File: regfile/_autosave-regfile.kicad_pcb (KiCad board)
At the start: 2 copper layers, 105.5 x 100 mm, 17 parts, among them J1 Conn_01x39_Pin, U1 74LS170, U1 74LS670, U11 74LS670, U12 74LS670, U13 74LS670, U14 74LS670, U18 74LS170, U2 74LS170, U2 74LS670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

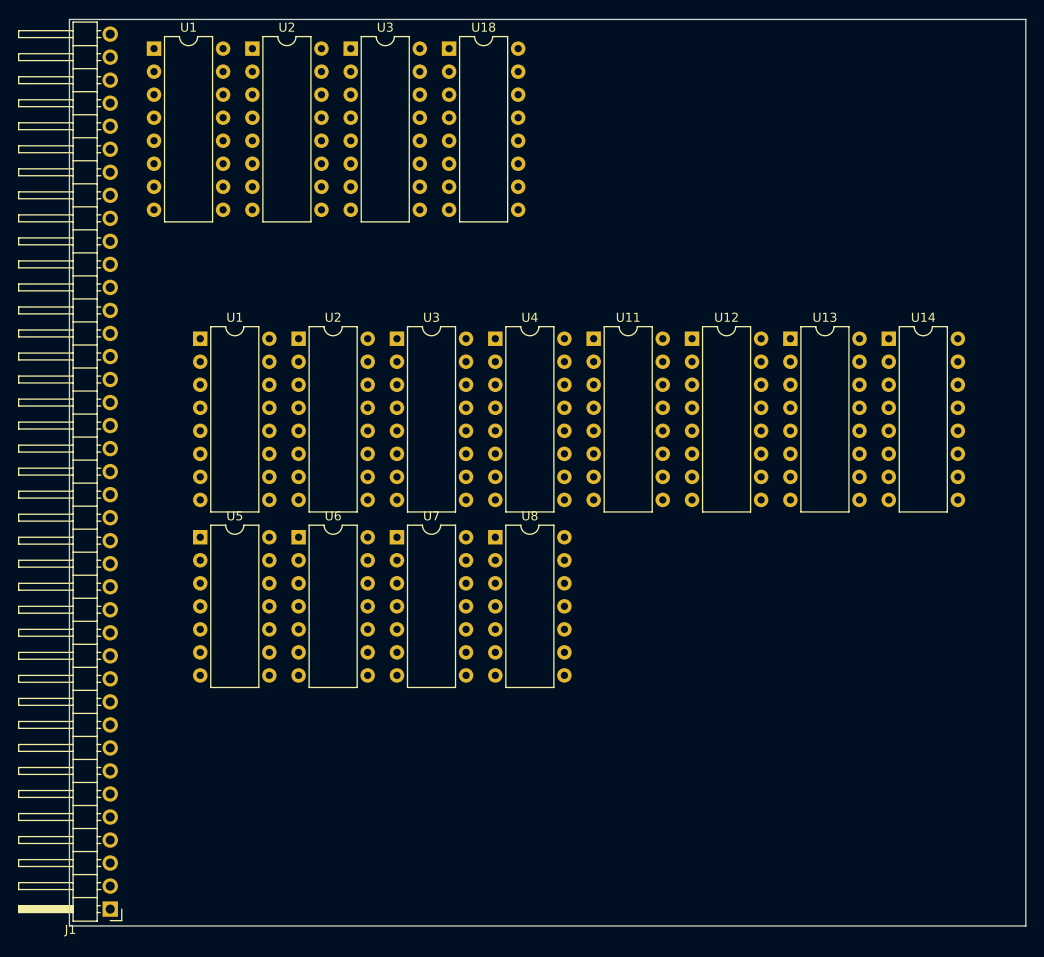
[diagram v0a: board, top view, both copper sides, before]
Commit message: fix logic for the regfile
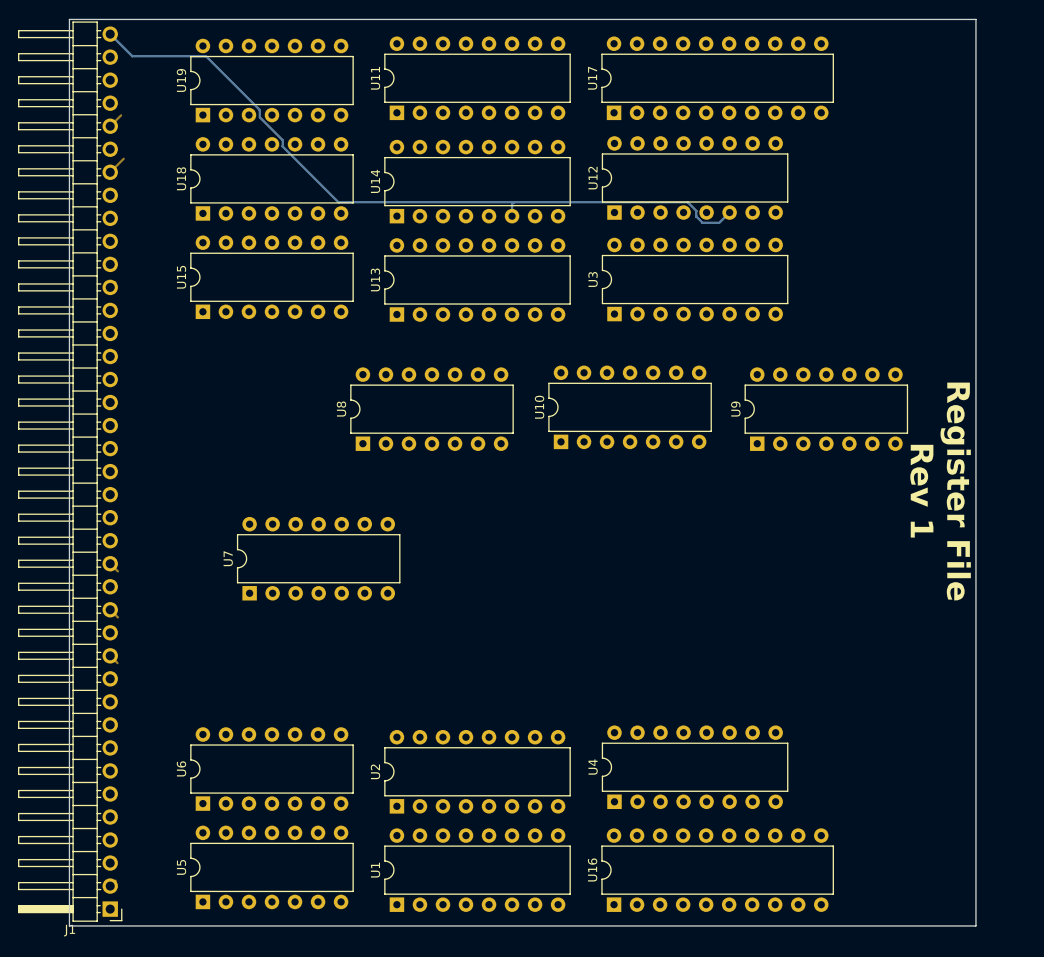
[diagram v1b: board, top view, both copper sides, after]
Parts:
- removed the U1 at (102.8, 39.2)
- removed the U1 at (107.9, 71.2)
- removed the U2 at (118.8, 71.2)
- removed the U2 at (113.7, 39.2)
- removed the U3 at (129.6, 71.2)
- removed the U3 at (124.5, 39.2)
- added U1: 74LS670, Package_DIP:DIP-16_W7.62mm, F.Cu at (129.6, 133.7)
- added U10: 74LS32, Package_DIP:DIP-14_W7.62mm, F.Cu at (147.7, 82.6)
- added U15: 74LS32, Package_DIP:DIP-14_W7.62mm, F.Cu at (108.2, 68.2)
- added U16: 74LS244, Package_DIP:DIP-20_W7.62mm, F.Cu at (153.6, 133.7)
- added U17: 74LS244, Package_DIP:DIP-20_W7.62mm, F.Cu at (153.6, 46.3)
- added U19: 74HC04, Package_DIP:DIP-14_W7.62mm, F.Cu at (108.2, 46.5)
- added U2: 74LS670, Package_DIP:DIP-16_W7.62mm, F.Cu at (129.6, 122.8)
- added U3: 74LS670, Package_DIP:DIP-16_W7.62mm, F.Cu at (153.6, 68.5)
- added U9: 74HC04, Package_DIP:DIP-14_W7.62mm, F.Cu at (169.4, 82.8)
- U18: value 74LS170 -> 74LS27; footprint Package_DIP:DIP-16_W7.62mm -> Package_DIP:DIP-14_W7.62mm
- moved U14 55.9 mm to (129.6, 57.7), turned to 90 degrees
- moved U4 52.7 mm to (153.6, 122.3), turned to 90 degrees
- moved U13 43.5 mm to (129.6, 68.5), turned to 90 degrees
- moved U5 40.2 mm to (108.2, 133.3), turned to 90 degrees
- moved U11 33.0 mm to (129.6, 46.3), turned to 90 degrees
- moved U18 32.7 mm to (108.2, 57.4), turned to 90 degrees
- moved U6 31.2 mm to (108.2, 122.5), turned to 90 degrees
- moved U8 17.9 mm to (125.9, 82.8), turned to 90 degrees
- moved U7 17.4 mm to (113.4, 99.3), turned to 90 degrees
- moved U12 16.3 mm to (153.6, 57.3), turned to 90 degrees
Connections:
- U14 pad 13: Net-(J1-Pin_7) -> Net-(J1-Pin_8)
- U18 pad 1: unconnected-(U18-D2-Pad1) -> Net-(J1-Pin_10)
- U18 pad 10: unconnected-(U18-Q1-Pad10) -> GND
- U18 pad 11: unconnected-(U18-~{Er}-Pad11) -> GND
- U18 pad 12: unconnected-(U18-~{Ew}-Pad12) -> ZR_addr1
- U18 pad 13: unconnected-(U18-Wb-Pad13) -> Net-(J1-Pin_12)
- U18 pad 14: unconnected-(U18-Wa-Pad14) -> +5V
- U18 pad 2: unconnected-(U18-D3-Pad2) -> Net-(J1-Pin_11)
- U18 pad 3: unconnected-(U18-D4-Pad3) -> Net-(J1-Pin_15)
- U18 pad 4: unconnected-(U18-Rb-Pad4) -> Net-(J1-Pin_14)
- U18 pad 5: unconnected-(U18-Ra-Pad5) -> Net-(J1-Pin_13)
- U18 pad 6: unconnected-(U18-Q4-Pad6) -> ZR_addr2
- U18 pad 7: unconnected-(U18-Q3-Pad7) -> GND
- U18 pad 8: GND -> unconnected-(U18-Pad8)
- U18 pad 9: unconnected-(U18-Q2-Pad9) -> GND
- U4 pad 13: Net-(J1-Pin_7) -> Net-(J1-Pin_8)
- U5 pad 10: Net-(J1-Pin_9) -> Net-(U5-Pad10)
- U5 pad 13: Net-(J1-Pin_12) -> unconnected-(U5-Pad13)
- U5 pad 2: Net-(J1-Pin_9) -> Net-(U5-Pad2)
- U5 pad 5: Net-(J1-Pin_12) -> Net-(U5-Pad5)
- U6 pad 11: Net-(U4-~{Er}) -> Net-(U10-Pad12)
- U7 pad 10: Net-(J1-Pin_9) -> Net-(U19-Pad2)
- U7 pad 11: Net-(U12-~{Er}) -> Net-(U15-Pad4)
- U7 pad 13: Net-(J1-Pin_15) -> Net-(U19-Pad4)
- U7 pad 2: Net-(J1-Pin_9) -> Net-(U7-Pad2)
- U7 pad 5: Net-(J1-Pin_15) -> Net-(U7-Pad5)
- U7 pad 6: Net-(U11-~{Er}) -> Net-(U15-Pad1)
- U8 pad 11: Net-(U14-~{Er}) -> Net-(U15-Pad12)
- U8 pad 6: Net-(U13-~{Er}) -> Net-(U15-Pad9)
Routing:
- net Net-(J1-Pin_39): track 0.00 -> 80.3 mm
- net Net-(J1-Pin_33): track 0.00 -> 2.11 mm
- net Net-(J1-Pin_35): track 0.00 -> 1.70 mm
- net Net-(J1-Pin_16): track 0.00 -> 1.20 mm
- net Net-(J1-Pin_14): track 0.00 -> 1.20 mm
- net Net-(J1-Pin_12): track 0.00 -> 1.13 mm
- net +5V: track 0.00 -> 0.85 mm
- net Net-(J1-Pin_28): track 0.00 -> 0.79 mm
- net Net-(J1-Pin_29): track 0.00 -> 0.74 mm
- net read enable 1: track 0.00 -> 0.74 mm
- net write enable: track 0.00 -> 0.58 mm
- net Net-(J1-Pin_7): track 0.00 -> 0.57 mm
- net Net-(J1-Pin_8): track 0.00 -> 0.51 mm
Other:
- board size 105.5 x 100 mm -> 100 x 100 mm
- board text added: "Register File Rev 1"
